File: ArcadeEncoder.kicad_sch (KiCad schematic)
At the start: 2 parts, among them J2 DB9_Male, U1 ProMicro

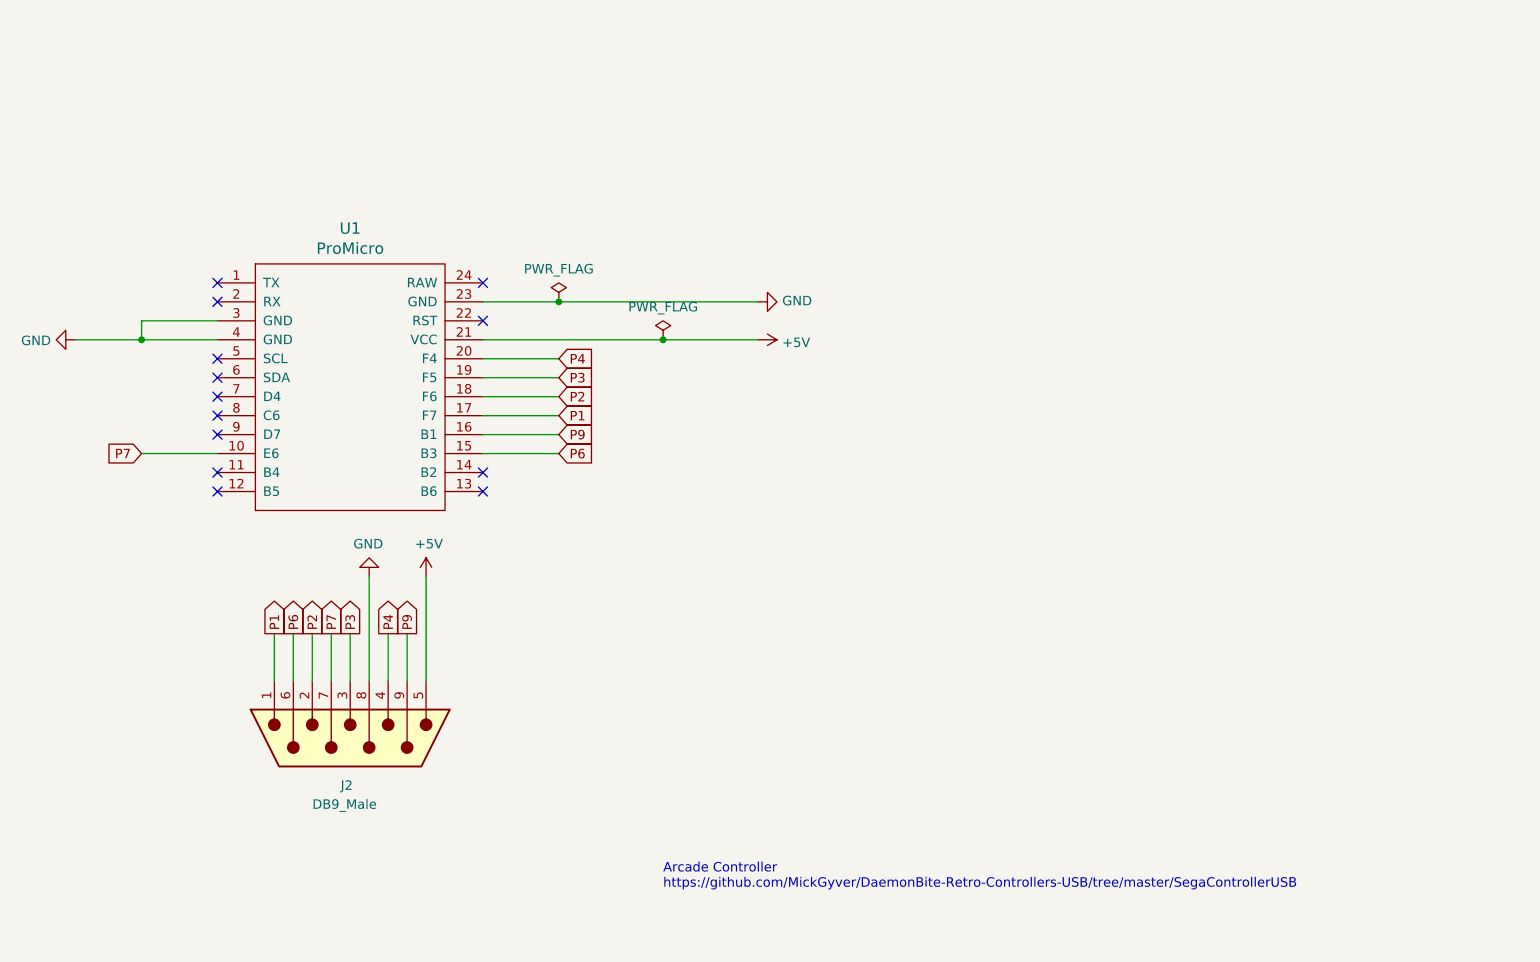
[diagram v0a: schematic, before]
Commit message: Sony PSX Connector
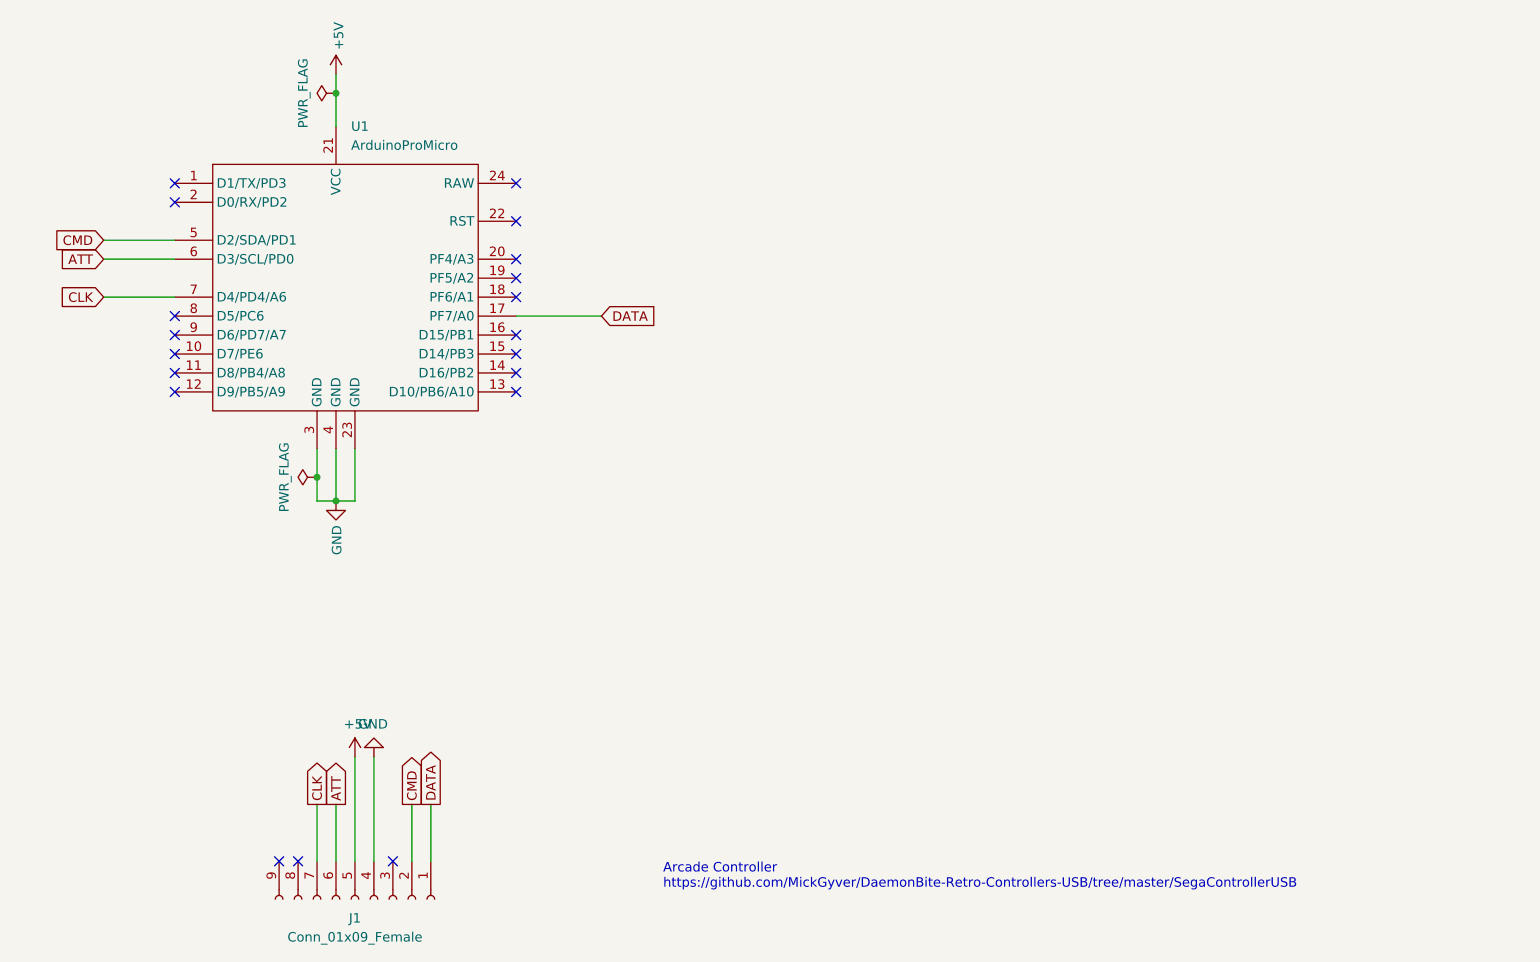
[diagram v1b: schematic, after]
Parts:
- removed J2: DB9_Male, haus-automatisierung:D-Sub_Connector_9P-Male, symbol Connector:DB9_Male
- removed U1: ProMicro, haus-automatisierung:ArduinoProMicro, symbol promicro:ProMicro
- added J1: Conn_01x09_Female, symbol Connector:Conn_01x09_Female
- added U1: ArduinoProMicro, haus-automatisierung:ArduinoProMicro, symbol haus-automatisierung:ArduinoProMicro
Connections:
- net +5V: now also J1.5 (Pin_5), U1.21 (VCC)
- net GND: now also J1.4 (Pin_4), U1.23 (GND), U1.3 (GND), U1.4 (GND)
- new net ATT: J1.6 (Pin_6), U1.6 (D3/SCL/PD0)
- new net CLK: J1.7 (Pin_7), U1.7 (D4/PD4/A6)
- new net CMD: J1.2 (Pin_2), U1.5 (D2/SDA/PD1)
- new net DATA: J1.1 (Pin_1), U1.17 (PF7/A0)
- no-connect marks 13 -> 19
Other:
- title: Arcade-Encoder (Sega) -> Arcade-Encoder (Sony)
